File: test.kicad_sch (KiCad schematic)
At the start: 17 parts, among them Q1 MMBT7002K

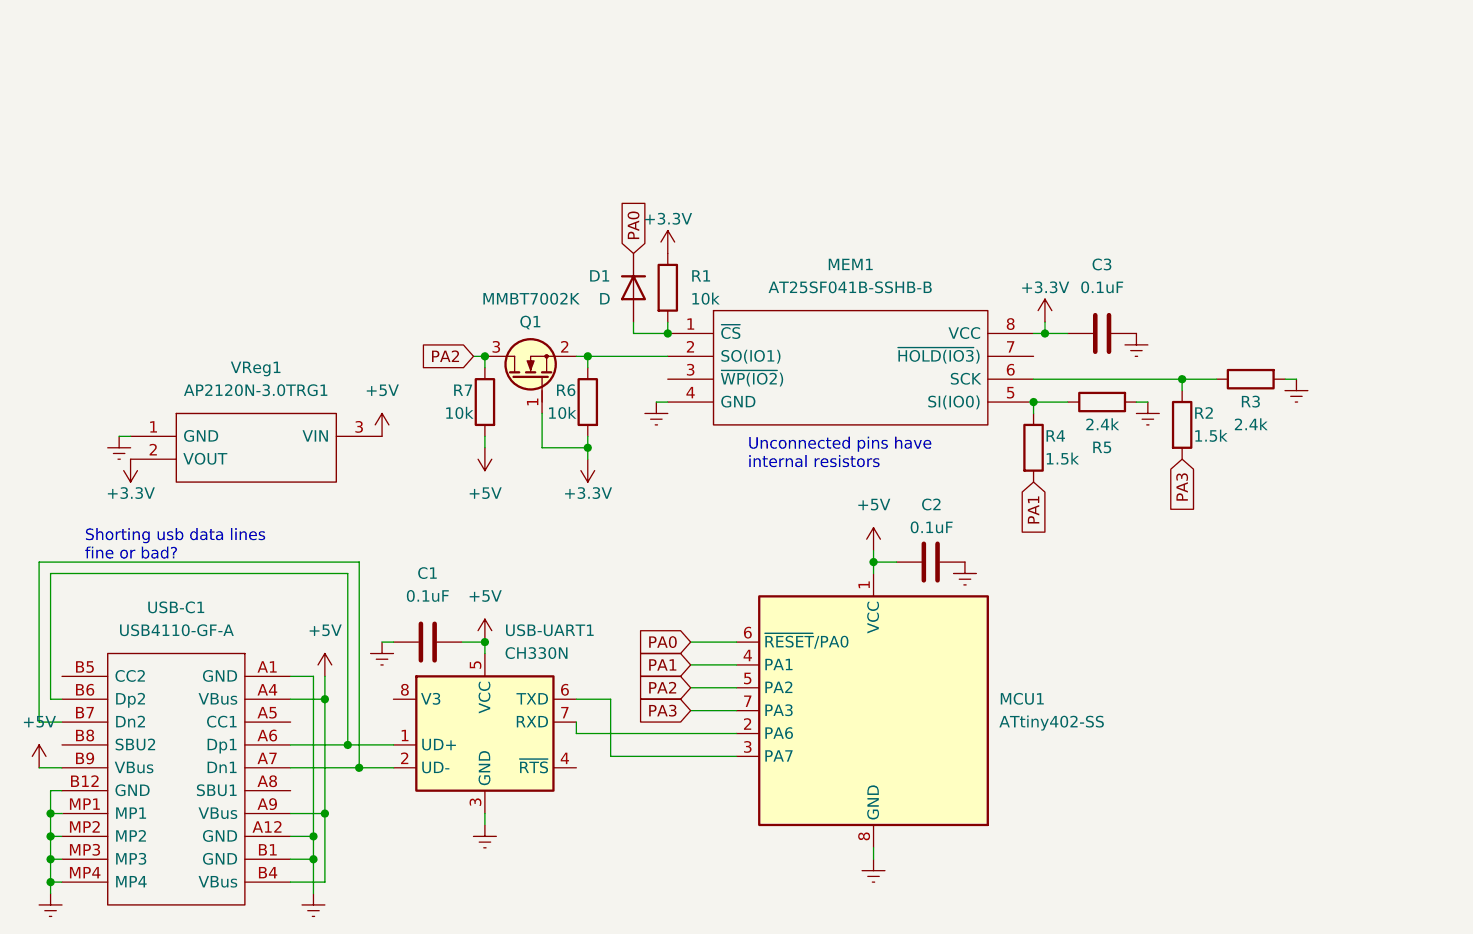
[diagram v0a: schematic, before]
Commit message: Rerouted with bigger traces, default usb receptacle symbol
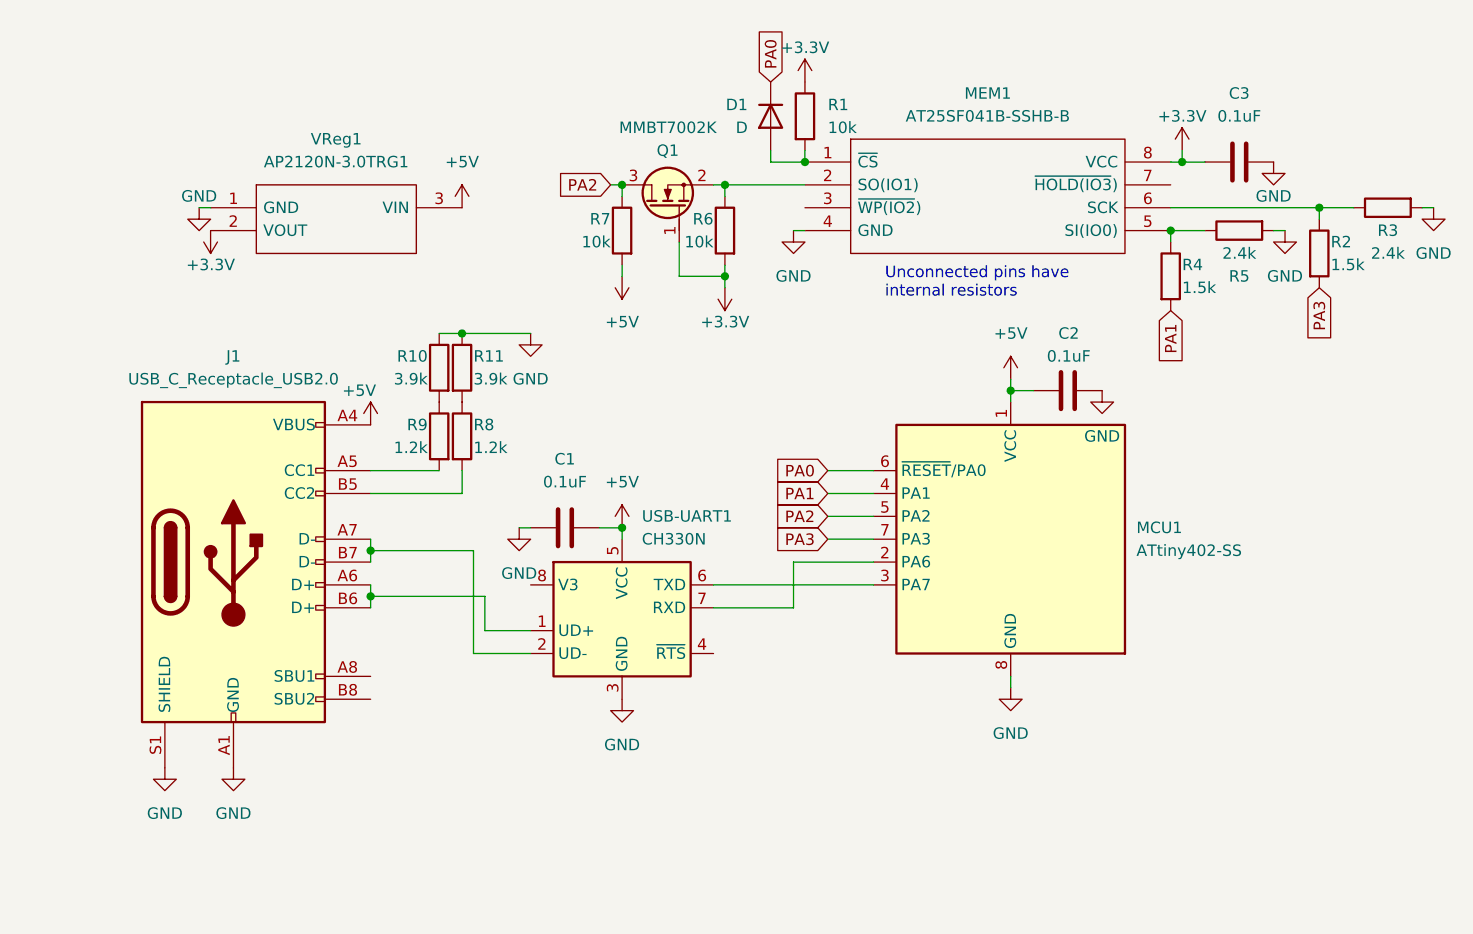
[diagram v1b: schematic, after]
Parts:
- removed USB-C1: USB4110-GF-A, Samacsys:USB4110GFA, symbol Samacsys:USB4110-GF-A
- added J1: USB_C_Receptacle_USB2.0, Samacsys:USB4110GFA_S, symbol Connector:USB_C_Receptacle_USB2.0
- added R10, R11: 3.9k, Resistor_SMD:R_0805_2012Metric, symbol Device:R
- added R8, R9: 1.2k, Resistor_SMD:R_0805_2012Metric, symbol Device:R
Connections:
- net +5V: now also J1.A4 (VBUS), J1.A9 (VBUS), J1.B4 (VBUS), J1.B9 (VBUS)
- net at USB-UART1.1 (UD+): now also J1.A6 (D+), J1.B6 (D+)
- net at USB-UART1.2 (UD-): now also J1.A7 (D-), J1.B7 (D-)
- net Earth renamed GND
- net GND: now also J1.A1 (GND), J1.A12 (GND), J1.B1 (GND), J1.B12 (GND), J1.S1 (SHIELD), R10.1, R11.1
- new net: R11.2, R8.1
- new net: J1.B5 (CC2), R8.2
- new net: J1.A5 (CC1), R9.2
- new net: R10.2, R9.1
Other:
- note removed: "Shorting usb data lines fine or bad?"
- moved on the sheet: C1, C2, C3, D1, MCU1, MEM1, Q1, R1, R2, R3, R4, R5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

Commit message: Programming pins
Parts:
- added J2: Conn_01x03, Connector_PinHeader_2.54mm:PinHeader_1x03_P2.54mm_Vertical, symbol Connector_Generic:Conn_01x03
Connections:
- net +5V: now also J2.1 (Pin_1)
- net GND: now also J2.2 (Pin_2)
- net PA0: now also J2.3 (Pin_3)
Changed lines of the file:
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@@
   (junction (at 63.5 69.85) (diameter 0) (color 0 0 0 0)
   )
+  (junction (at 102.87 85.09) (diameter 0) (color 0 0 0 0)
+  )
   (junction (at 158.75 55.88) (diameter 0) (color 0 0 0 0)
   )
@@
     (stroke (width 0) (type default))
   )
-  (wire (pts (xy 104.14 85.09) (xy 109.22 85.09))
+  (wire (pts (xy 101.6 85.09) (xy 102.87 85.09))
     (stroke (width 0) (type default))
   )
@@
     (stroke (width 0) (type default))
   )
+  (wire (pts (xy 100.33 74.93) (xy 102.87 74.93))
+    (stroke (width 0) (type default))
+  )
   (wire (pts (xy 53.34 93.98) (xy 53.34 95.25))
     (stroke (width 0) (type default))
@@
     (stroke (width 0) (type default))
   )
+  (wire (pts (xy 100.33 72.39) (xy 102.87 72.39))
+    (stroke (width 0) (type default))
+  )
   (wire (pts (xy 104.14 87.63) (xy 109.22 87.63))
     (stroke (width 0) (type default))
@@
   )
   (wire (pts (xy 92.71 62.23) (xy 92.71 63.5))
+    (stroke (width 0) (type default))
+  )
+  (wire (pts (xy 102.87 77.47) (xy 102.87 85.09))
+    (stroke (width 0) (type default))
+  )
+  (wire (pts (xy 102.87 85.09) (xy 109.22 85.09))
     (stroke (width 0) (type default))
   )
@@
     )
   )
-  (global_label "PA0" (shape input) (at 104.14 85.09 180) (fields_autoplaced)
+  (global_label "PA0" (shape input) (at 101.6 85.09 180) (fields_autoplaced)
     (effects (font (size 1.27 1.27)) (justify right))
-    (property "Intersheetrefs" "${INTERSHEET_REFS}" (at 97.5867 85.09 0)
+    (property "Intersheetrefs" "${INTERSHEET_REFS}" (at 95.0467 85.09 0)
       (effects (font (size 1.27 1.27)) (justify right) hide)
     )
@@
     )
   )
+  (symbol (lib_id "power:GND") (at 100.33 74.93 0) (unit 1)
+    (in_bom yes) (on_board yes) (dnp no) (fields_autoplaced)
+    (property "Reference" "#PWR022" (at 100.33 81.28 0)
+      (effects (font (size 1.27 1.27)) hide)
+    )
+    (property "Value" "GND" (at 100.33 80.01 0)
+      (effects (font (size 1.27 1.27)))
+    )
+    (property "Footprint" "" (at 100.33 74.93 0)
+      (effects (font (size 1.27 1.27)) hide)
+    )
+    (property "Datasheet" "" (at 100.33 74.93 0)
+      (effects (font (size 1.27 1.27)) hide)
+    )
+    (pin "1")
+    (instances
+      (project "test"
+        (path "/85284967-e784-4878-80b8-698860f0397b"
+          (reference "#PWR022") (unit 1)
+        )
+      )
+    )
+  )
   (symbol (lib_id "power:+5V") (at 81.28 63.5 180) (unit 1)
     (in_bom yes) (on_board yes) (dnp no) (fields_autoplaced)
@@
     )
   )
+  (symbol (lib_id "Connector_Generic:Conn_01x03") (at 107.95 74.93 0) (unit 1)
+    (in_bom yes) (on_board yes) (dnp no) (fields_autoplaced)
+    (property "Reference" "J2" (at 110.49 73.66 0)
+      (effects (font (size 1.27 1.27)) (justify left))
+    )
+    (property "Value" "Conn_01x03" (at 110.49 76.2 0)
+      (effects (font (size 1.27 1.27)) (justify left))
+    )
+    (property "Footprint" "Connector_PinHeader_2.54mm:PinHeader_1x03_P2.54mm_Vertical" (at 107.95 74.93 0)
+      (effects (font (size 1.27 1.27)) hide)
+    )
+    (property "Datasheet" "~" (at 107.95 74.93 0)
+      (effects (font (size 1.27 1.27)) hide)
+    )
+    (pin "3")
+    (pin "2")
+    (pin "1")
+    (instances
+      (project "test"
+        (path "/85284967-e784-4878-80b8-698860f0397b"
+          (reference "J2") (unit 1)
+        )
+      )
+    )
+  )
   (symbol (lib_id "power:GND") (at 30.48 118.11 0) (unit 1)
     (in_bom yes) (on_board yes) (dnp no) (fields_autoplaced)
@@
         )
       )
+    )
+  )
+  (symbol (lib_id "power:+5V") (at 100.33 72.39 0) (unit 1)
+    (in_bom yes) (on_board yes) (dnp no) (fields_autoplaced)
+    (property "Reference" "#PWR016" (at 100.33 76.2 0)
+      (effects (font (size 1.27 1.27)) hide)
+    )
+    (property "Value" "+5V" (at 100.33 67.31 0)
+      (effects (font (size 1.27 1.27)))
+    )
+    (property "Footprint" "" (at 100.33 72.39 0)
+      (effects (font (size 1.27 1.27)) hide)
+    )
+    (property "Datasheet" "" (at 100.33 72.39 0)
+      (effects (font (size 1.27 1.27)) hide)
+    )
+    (pin "1")
+    (instances
+      (project "test"
+        (path "/85284967-e784-4878-80b8-698860f0397b"
+          (reference "#PWR016") (unit 1)
+        )
+      )
